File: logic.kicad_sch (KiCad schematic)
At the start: 57 parts, among them J5 HanRun_HR911105A, Q24 2N7002, Q25 AO3401A, Q26 AO3401A, Q27 2N7002, U10 LAN8720A, U11 74HC595, U8 SY8120B1ABC, U9 ESP32-WROOM-32E

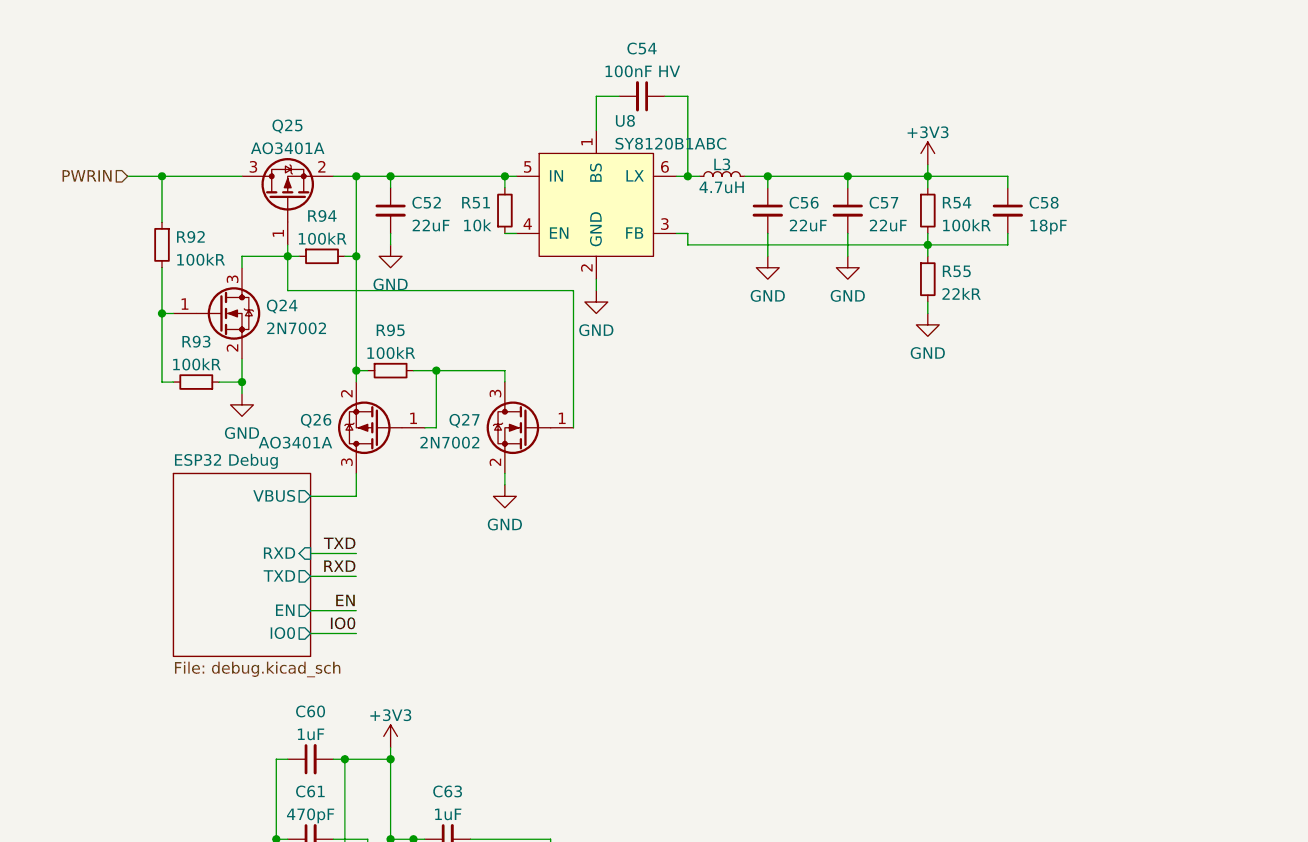
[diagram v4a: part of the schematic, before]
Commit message: Charger and step-down component placement
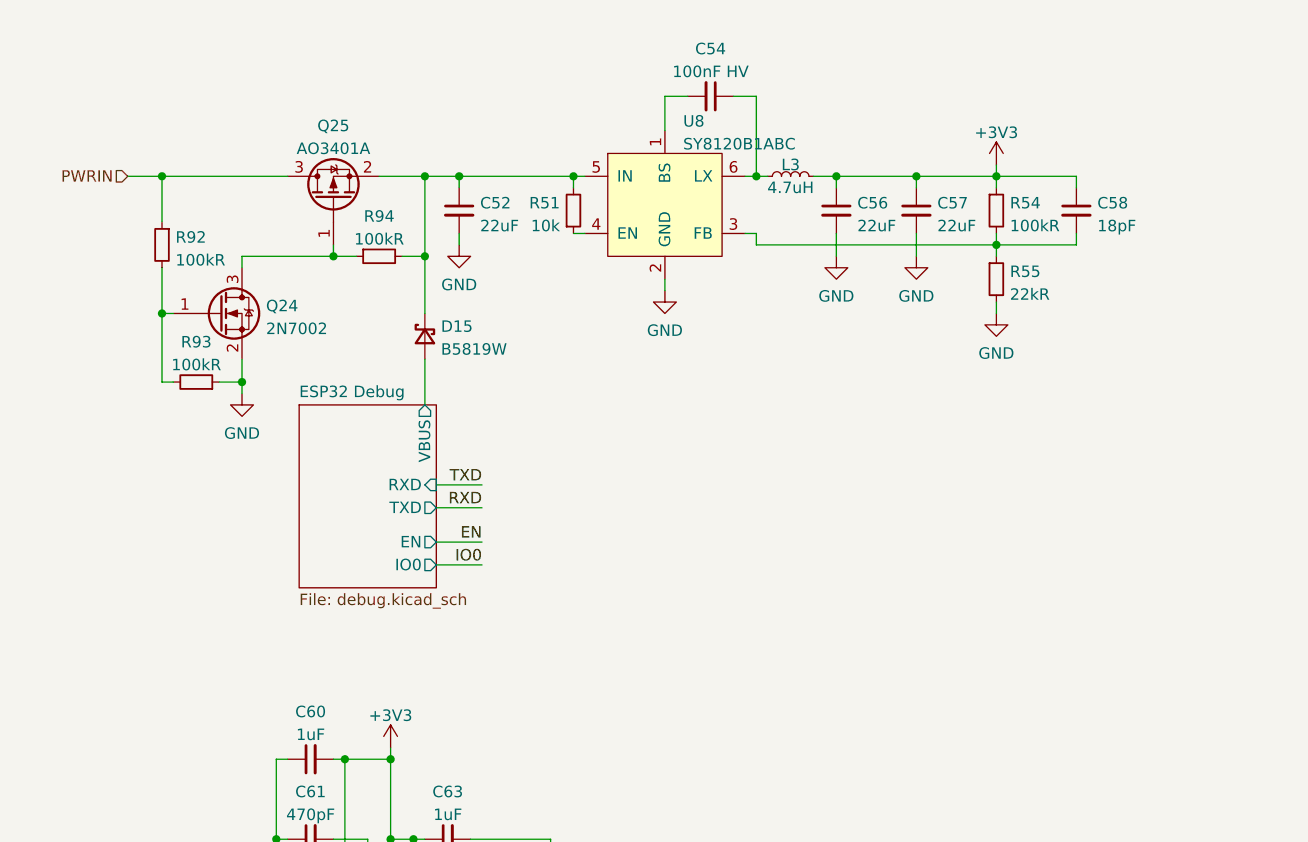
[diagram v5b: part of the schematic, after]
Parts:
- removed Q26: AO3401A, Package_TO_SOT_SMD:SOT-23, symbol Transistor_FET:AO3401A
- removed Q27: 2N7002, Package_TO_SOT_SMD:SOT-23, symbol Transistor_FET:2N7002
- removed R95: 100kR, Resistor_SMD:R_0402_1005Metric, symbol Device:R_Small
- added D15: B5819W, Diode_SMD:D_SOD-123, symbol Device:D_Schottky_Small
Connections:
- net ESP32 Debug/VBUS: now also D15.2 (A)
- net at C52.1, Q25.2 (S), R51.2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: now also D15.1 (K)
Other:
- moved on the sheet: C52, C54, C56, C57, C58, L3, Q25, R51, R54, R55, R94, U8

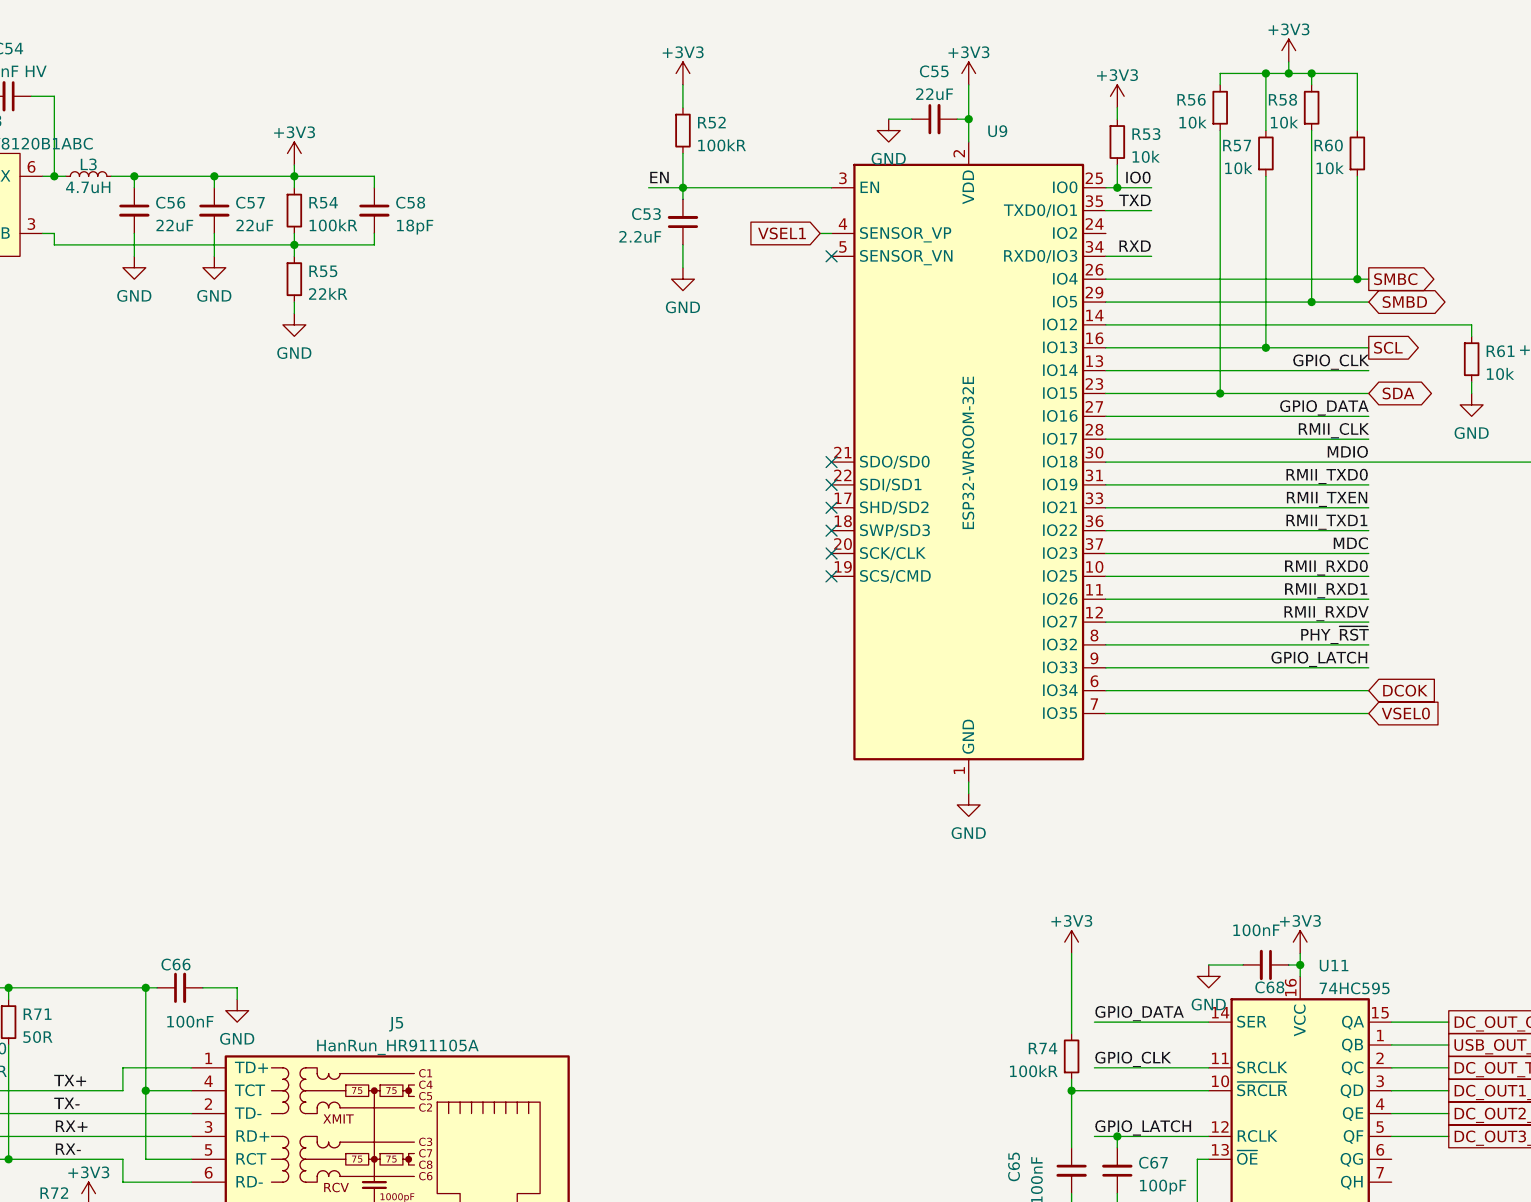
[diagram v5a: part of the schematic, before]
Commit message: Add 64x48 SSD1306 OLED
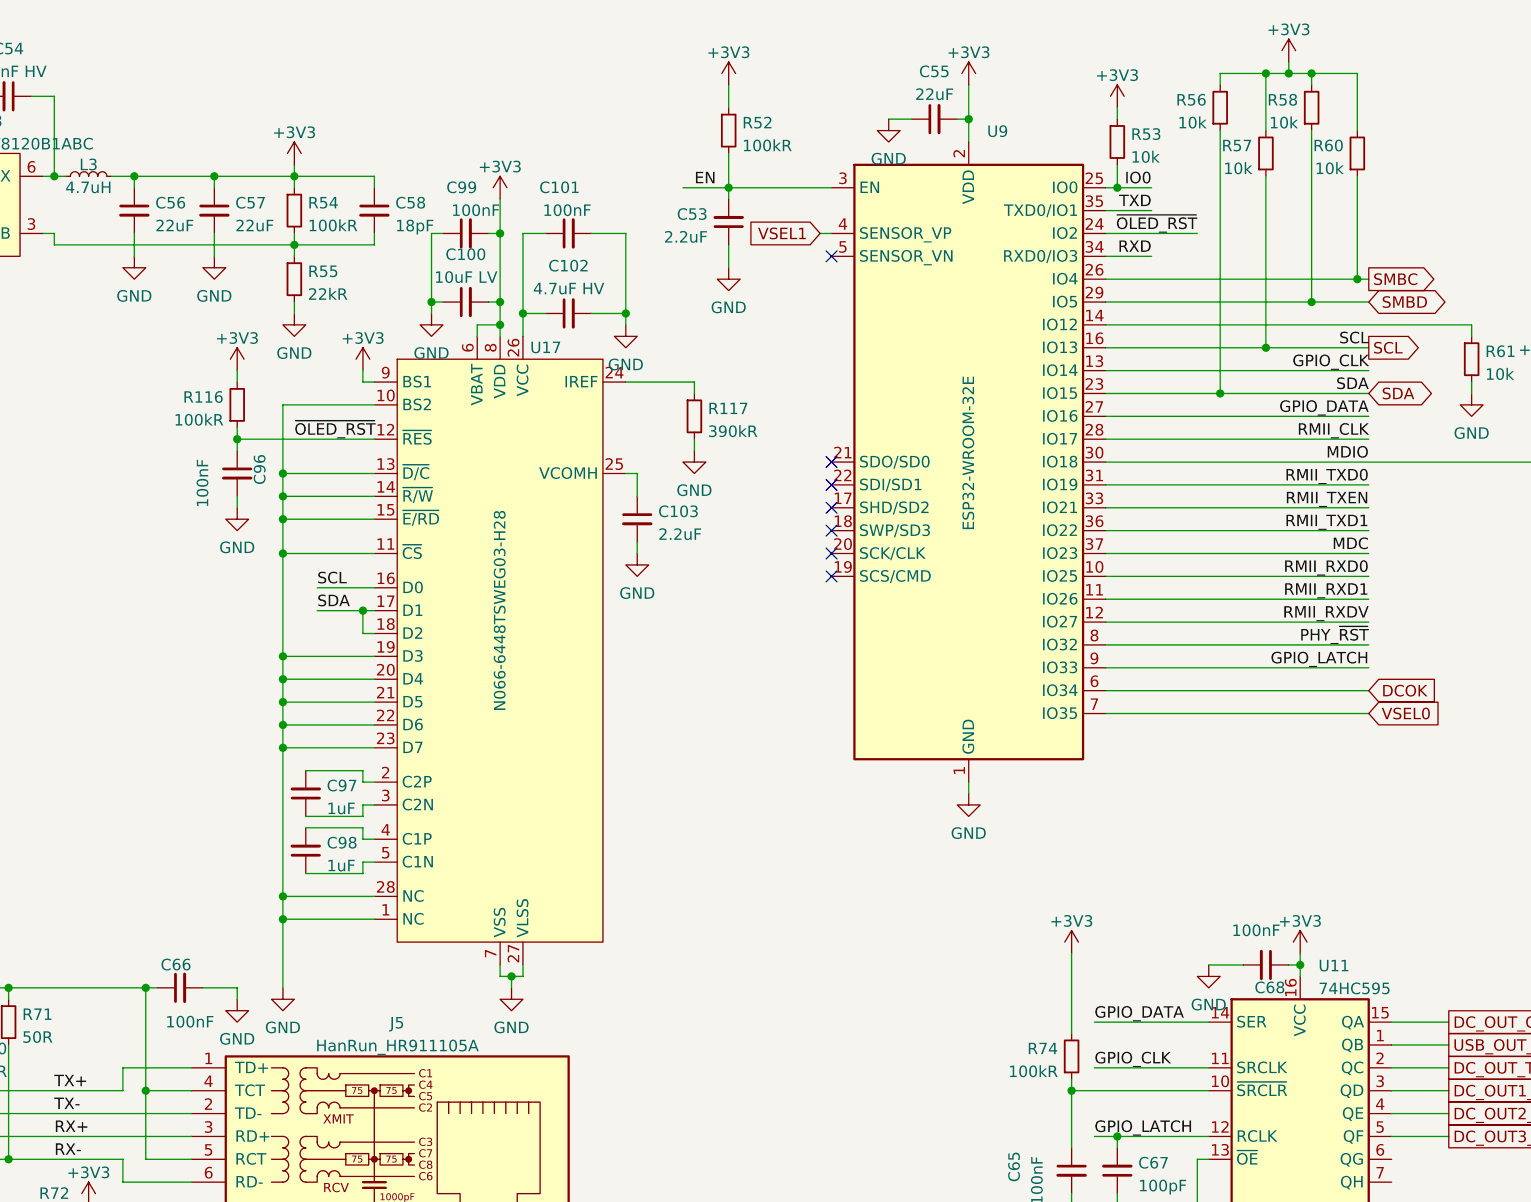
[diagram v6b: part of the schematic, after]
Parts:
- added C100: 10uF LV, Capacitor_SMD:C_0402_1005Metric, symbol Device:C_Small
- added C101, C96, C99: 100nF, Capacitor_SMD:C_0402_1005Metric, symbol Device:C_Small
- added C102: 4.7uF HV, Capacitor_SMD:C_0603_1608Metric, symbol Device:C_Small
- added C103: 2.2uF, Capacitor_SMD:C_0603_1608Metric, symbol Device:C_Small
- added C97, C98: 1uF, Capacitor_SMD:C_0402_1005Metric, symbol Device:C_Small
- added R116: 100kR, Resistor_SMD:R_0402_1005Metric, symbol Device:R_Small
- added R117: 390kR, Resistor_SMD:R_0603_1608Metric, symbol Device:R_Small
- added U17: N066-6448TSWEG03-H28, Display_OLED:N066-6448TSWEG03-H28, symbol Display_OLED:N066-6448TSWEG03-H28
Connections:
- net +3V3: now also C100.2, C99.2, R116.2, U17.6 (VBAT), U17.8 (VDD), U17.9 (BS1)
- net GND: now also C100.1, C101.2, C102.2, C103.2, C96.2, C99.1, R117.2, U17.1 (NC), U17.10 (BS2), U17.11 (~{CS}), U17.13 (~{D/C}), U17.14 (~{R/W}), U17.15 (~{E/RD}), U17.19 (D3), U17.20 (D4), U17.21 (D5), U17.22 (D6), U17.23 (D7), U17.27 (VLSS), U17.28 (NC), U17.7 (VSS)
- net SCL: now also U17.16 (D0)
- net SDA: now also U17.17 (D1), U17.18 (D2)
- net ~{OLED_RST}: now reaches U9.24 (IO2)
- net ~{OLED_RST}: now also C96.1, R116.1, U17.12 (~{RES})
- new net: C97.2, U17.2 (C2P)
- new net: R117.1, U17.24 (IREF)
- new net: C103.1, U17.25 (VCOMH)
- new net: C101.1, C102.1, U17.26 (VCC)
- new net: C97.1, U17.3 (C2N)
- new net: C98.2, U17.4 (C1P)
- new net: C98.1, U17.5 (C1N)
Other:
- moved on the sheet: C53, R52

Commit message: Plan front panel element positioning
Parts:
- added R?: 10k, Resistor_SMD:R_0402_1005Metric, symbol Device:R_Small
- added SW?: SW_Push, Button_Switch_SMD_LCSC:x-1825027-x, symbol Switch_MountingPin:SW_Push_MountingPin
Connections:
- net +3V3: now also R?.1
- net GND: now also SW?.2, SW?.MP
- net BUTTON: now reaches U9.5 (SENSOR_VN)
- net BUTTON: now also R?.2, SW?.1
- no-connect marks 10 -> 9
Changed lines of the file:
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@@
   (junction (at 41.91 119.38) (diameter 0) (color 0 0 0 0)
   )
+  (junction (at 271.78 78.74) (diameter 0) (color 0 0 0 0)
+  )
   (junction (at 135.89 90.17) (diameter 0) (color 0 0 0 0)
   )
@@
   (no_connect (at 259.08 151.13))
   (no_connect (at 49.53 168.91))
-  (no_connect (at 196.85 43.18))
   (no_connect (at 49.53 146.05))
   (no_connect (at 196.85 66.04))
@@
     (stroke (width 0) (type default) (color 0 0 0 0))
   )
+  (wire (pts (xy 195.58 43.18) (xy 196.85 43.18))
+    (stroke (width 0) (type default) (color 0 0 0 0))
+  )
   (wire (pts (xy 63.5 43.18) (xy 66.04 43.18))
     (stroke (width 0) (type default) (color 0 0 0 0))
@@
     (stroke (width 0) (type default) (color 0 0 0 0))
   )
+  (wire (pts (xy 271.78 78.74) (xy 271.78 80.01))
+    (stroke (width 0) (type default) (color 0 0 0 0))
+  )
   (wire (pts (xy 248.92 157.48) (xy 237.49 157.48))
     (stroke (width 0) (type default) (color 0 0 0 0))
@@
     (stroke (width 0) (type default) (color 0 0 0 0))
   )
+  (wire (pts (xy 271.78 71.12) (xy 271.78 72.39))
+    (stroke (width 0) (type default) (color 0 0 0 0))
+  )
   (wire (pts (xy 146.05 41.91) (xy 146.05 40.64))
     (stroke (width 0) (type default) (color 0 0 0 0))
@@
     (stroke (width 0) (type default) (color 0 0 0 0))
   )
+  (wire (pts (xy 266.7 85.09) (xy 267.97 85.09))
+    (stroke (width 0) (type default) (color 0 0 0 0))
+  )
   (wire (pts (xy 165.1 40.64) (xy 162.56 40.64))
     (stroke (width 0) (type default) (color 0 0 0 0))
@@
     (stroke (width 0) (type default) (color 0 0 0 0))
   )
+  (wire (pts (xy 271.78 77.47) (xy 271.78 78.74))
+    (stroke (width 0) (type default) (color 0 0 0 0))
+  )
   (wire (pts (xy 146.05 63.5) (xy 130.81 63.5))
     (stroke (width 0) (type default) (color 0 0 0 0))
@@
     (stroke (width 0) (type default) (color 0 0 0 0))
   )
+  (wire (pts (xy 195.58 43.18) (xy 195.58 44.45))
+    (stroke (width 0) (type default) (color 0 0 0 0))
+  )
   (wire (pts (xy 135.89 87.63) (xy 135.89 90.17))
     (stroke (width 0) (type default) (color 0 0 0 0))
@@
     (stroke (width 0) (type default) (color 0 0 0 0))
   )
+  (wire (pts (xy 266.7 86.36) (xy 266.7 85.09))
+    (stroke (width 0) (type default) (color 0 0 0 0))
+  )
   (wire (pts (xy 226.06 128.27) (xy 238.76 128.27))
     (stroke (width 0) (type default) (color 0 0 0 0))
@@
     (stroke (width 0) (type default) (color 0 0 0 0))
   )
+  (wire (pts (xy 187.96 44.45) (xy 195.58 44.45))
+    (stroke (width 0) (type default) (color 0 0 0 0))
+  )
   (wire (pts (xy 100.33 29.21) (xy 100.33 25.4))
     (stroke (width 0) (type default) (color 0 0 0 0))
@@
     (stroke (width 0) (type default) (color 0 0 0 0))
   )
+  (wire (pts (xy 262.89 78.74) (xy 271.78 78.74))
+    (stroke (width 0) (type default) (color 0 0 0 0))
+  )
   (wire (pts (xy 223.52 120.65) (xy 223.52 129.54))
     (stroke (width 0) (type default) (color 0 0 0 0))
@@
     (stroke (width 0) (type default) (color 0 0 0 0))
   )
+  (wire (pts (xy 271.78 90.17) (xy 271.78 91.44))
+    (stroke (width 0) (type default) (color 0 0 0 0))
+  )
   (wire (pts (xy 69.85 107.95) (xy 69.85 99.06))
     (stroke (width 0) (type default) (color 0 0 0 0))
@@
     (effects (font (size 1.27 1.27)) (justify right bottom))
   )
+  (label "BUTTON" (at 262.89 78.74 0)
+    (effects (font (size 1.27 1.27)) (justify left bottom))
+  )
   (label "PHY_~{RST}" (at 256.54 86.36 180)
     (effects (font (size 1.27 1.27)) (justify right bottom))
@@
     (effects (font (size 1.27 1.27)) (justify left bottom))
   )
+  (label "BUTTON" (at 187.96 44.45 0)
+    (effects (font (size 1.27 1.27)) (justify left bottom))
+  )
   (label "MDIO" (at 24.13 151.13 0)
     (effects (font (size 1.27 1.27)) (justify left bottom))
@@
     (pin "1")
   )
+  (symbol (lib_id "power:GND") (at 266.7 86.36 0) (unit 1)
+    (in_bom yes) (on_board yes) (fields_autoplaced)
+    (property "Reference" "#PWR?" (id 0) (at 266.7 92.71 0)
+      (effects (font (size 1.27 1.27)) hide)
+    )
+    (property "Value" "GND" (id 1) (at 266.7 90.8034 0))
+    (property "Footprint" "" (id 2) (at 266.7 86.36 0)
+      (effects (font (size 1.27 1.27)) hide)
+    )
+    (property "Datasheet" "" (id 3) (at 266.7 86.36 0)
+      (effects (font (size 1.27 1.27)) hide)
+    )
+    (pin "1")
+  )
   (symbol (lib_id "power:GND") (at 185.42 44.45 0) (unit 1)
     (in_bom yes) (on_board yes) (fields_autoplaced)
@@
     (pin "1")
   )
+  (symbol (lib_id "power:+3V3") (at 271.78 71.12 0) (unit 1)
+    (in_bom yes) (on_board yes) (fields_autoplaced)
+    (property "Reference" "#PWR?" (id 0) (at 271.78 74.93 0)
+      (effects (font (size 1.27 1.27)) hide)
+    )
+    (property "Value" "+3V3" (id 1) (at 271.78 67.5442 0))
+    (property "Footprint" "" (id 2) (at 271.78 71.12 0)
+      (effects (font (size 1.27 1.27)) hide)
+    )
+    (property "Datasheet" "" (id 3) (at 271.78 71.12 0)
+      (effects (font (size 1.27 1.27)) hide)
+    )
+    (pin "1")
+  )
   (symbol (lib_id "power:+3V3") (at 212.09 24.13 0) (unit 1)
     (in_bom yes) (on_board yes) (fields_autoplaced)
@@
     (pin "2")
   )
+  (symbol (lib_id "Device:R_Small") (at 271.78 74.93 0) (unit 1)
+    (in_bom yes) (on_board yes) (fields_autoplaced)
+    (property "Reference" "R?" (id 0) (at 273.2786 74.0953 0)
+      (effects (font (size 1.27 1.27)) (justify left))
+    )
+    (property "Value" "10k" (id 1) (at 273.2786 76.6322 0)
+      (effects (font (size 1.27 1.27)) (justify left))
+    )
+    (property "Footprint" "Resistor_SMD:R_0402_1005Metric" (id 2) (at 271.78 74.93 0)
+      (effects (font (size 1.27 1.27)) hide)
+    )
+    (property "Datasheet" "~" (id 3) (at 271.78 74.93 0)
+      (effects (font (size 1.27 1.27)) hide)
+    )
+    (property "LCSC" "C25744" (id 4) (at 271.78 74.93 0)
+      (effects (font (size 1.27 1.27)) hide)
+    )
+    (pin "1")
+    (pin "2")
+  )
   (symbol (lib_id "power:+3V3") (at 160.02 36.83 0) (unit 1)
     (in_bom yes) (on_board yes) (fields_autoplaced)
@@
     (pin "2")
   )
+  (symbol (lib_id "power:GND") (at 271.78 91.44 0) (unit 1)
+    (in_bom yes) (on_board yes) (fields_autoplaced)
+    (property "Reference" "#PWR?" (id 0) (at 271.78 97.79 0)
+      (effects (font (size 1.27 1.27)) hide)
+    )
+    (property "Value" "GND" (id 1) (at 271.78 95.8834 0))
+    (property "Footprint" "" (id 2) (at 271.78 91.44 0)
+      (effects (font (size 1.27 1.27)) hide)
+    )
+    (property "Datasheet" "" (id 3) (at 271.78 91.44 0)
+      (effects (font (size 1.27 1.27)) hide)
+    )
+    (pin "1")
+  )
   (symbol (lib_id "Device:R_Small") (at 105.41 128.27 0) (unit 1)
     (in_bom yes) (on_board yes) (fields_autoplaced)
@@
     (pin "1")
   )
+  (symbol (lib_id "Switch_MountingPin:SW_Push_MountingPin") (at 271.78 85.09 270) (unit 1)
+    (in_bom yes) (on_board yes) (fields_autoplaced)
+    (property "Reference" "SW?" (id 0) (at 275.463 84.2553 90)
+      (effects (font (size 1.27 1.27)) (justify left))
+    )
+    (property "Value" "SW_Push" (id 1) (at 275.463 86.7922 90)
+      (effects (font (size 1.27 1.27)) (justify left))
+    )
+    (property "Footprint" "Button_Switch_SMD_LCSC:x-1825027-x" (id 2) (at 271.78 85.09 0)
+      (effects (font (size 1.27 1.27)) hide)
+    )
+    (property "Datasheet" "https://datasheet.lcsc.com/szlcsc/1811132015_TE-Connectivity-1-1825027-1_C266183.pdf" (id 3) (at 271.78 85.09 0)
+      (effects (font (size 1.27 1.27)) hide)
+    )
+    (property "LCSC" "C266183" (id 4) (at 271.78 85.09 90)
+      (effects (font (size 1.27 1.27)) hide)
+    )
+    (pin "1")
+    (pin "2")
+    (pin "MP")
+  )
   (symbol (lib_id "Device:C_Small") (at 60.96 99.06 90) (unit 1)
